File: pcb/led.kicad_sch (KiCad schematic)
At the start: 7 parts, among them Q1 DTC143X, Q2 DTC143X, Q3 DTC143X

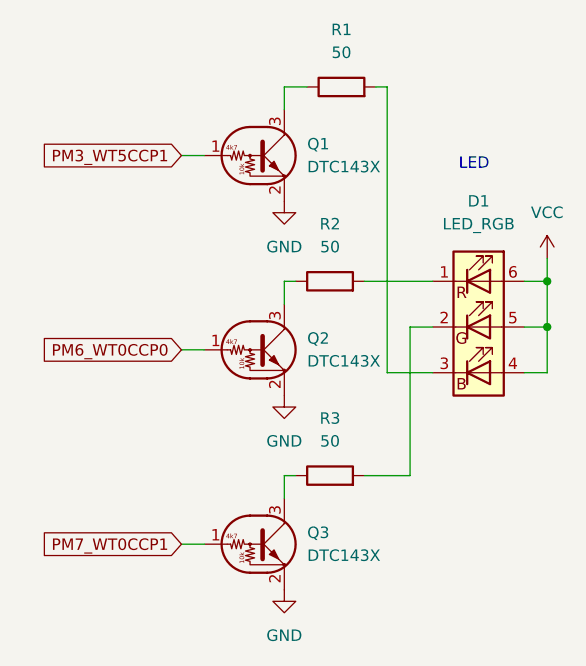
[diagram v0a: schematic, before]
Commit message: Add hardware encoder support
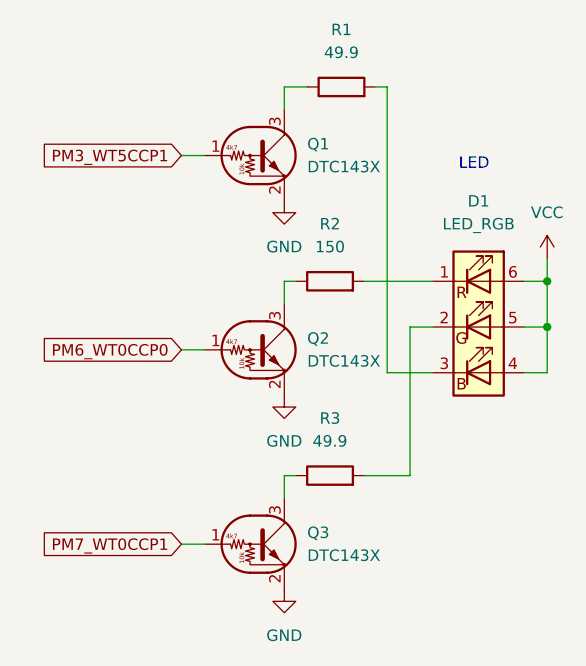
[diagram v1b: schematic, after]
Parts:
- R1, R3: value 50 -> 49.9
- R2: value 50 -> 150
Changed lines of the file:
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@@
 			)
 		)
-		(property "Value" "50"
+		(property "Value" "49.9"
 			(at 149.86 109.22 90)
 			(effects
@@
 			)
 		)
-		(property "Value" "50"
+		(property "Value" "150"
 			(at 149.86 87.63 90)
 			(effects
@@
 			)
 		)
-		(property "Value" "50"
+		(property "Value" "49.9"
 			(at 151.13 66.04 90)
 			(effects
